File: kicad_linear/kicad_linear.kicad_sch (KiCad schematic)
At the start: 6 parts, among them J1 LObits, J2 HIbits, J3 PGM, U1 ATtiny1616-S, U2 HSN-3621

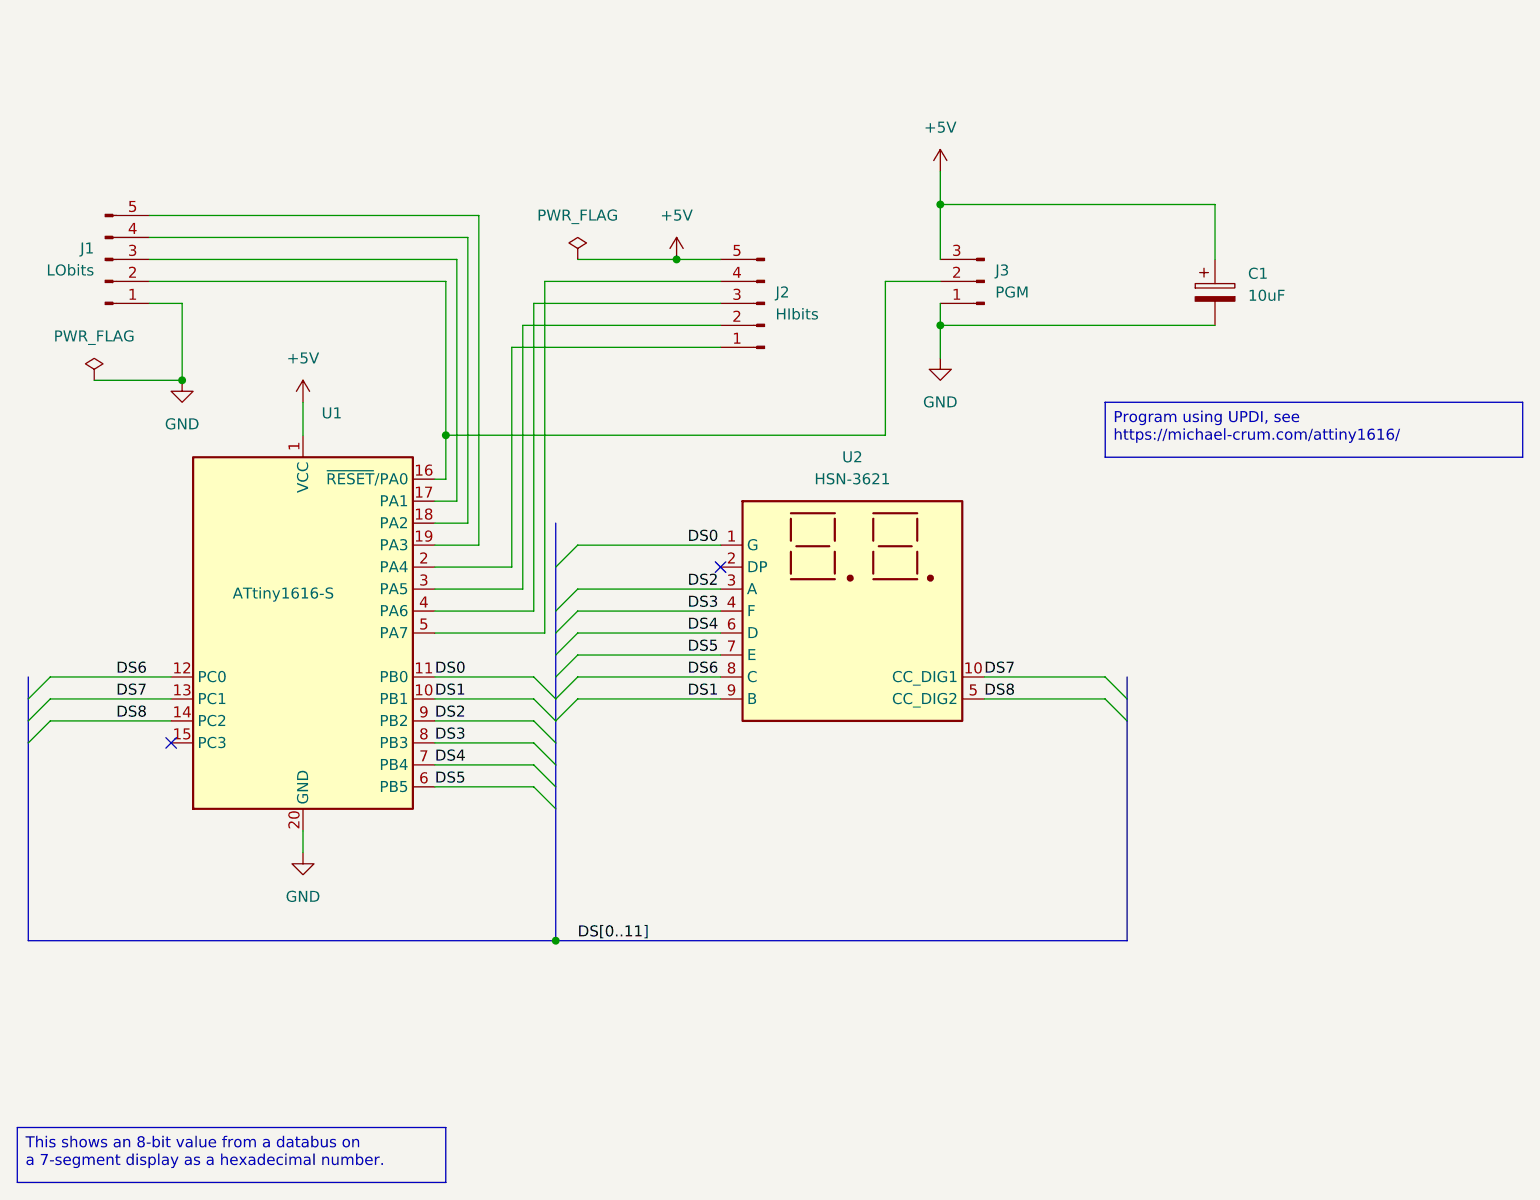
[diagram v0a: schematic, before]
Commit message: Add a linear variant that should be easier to use
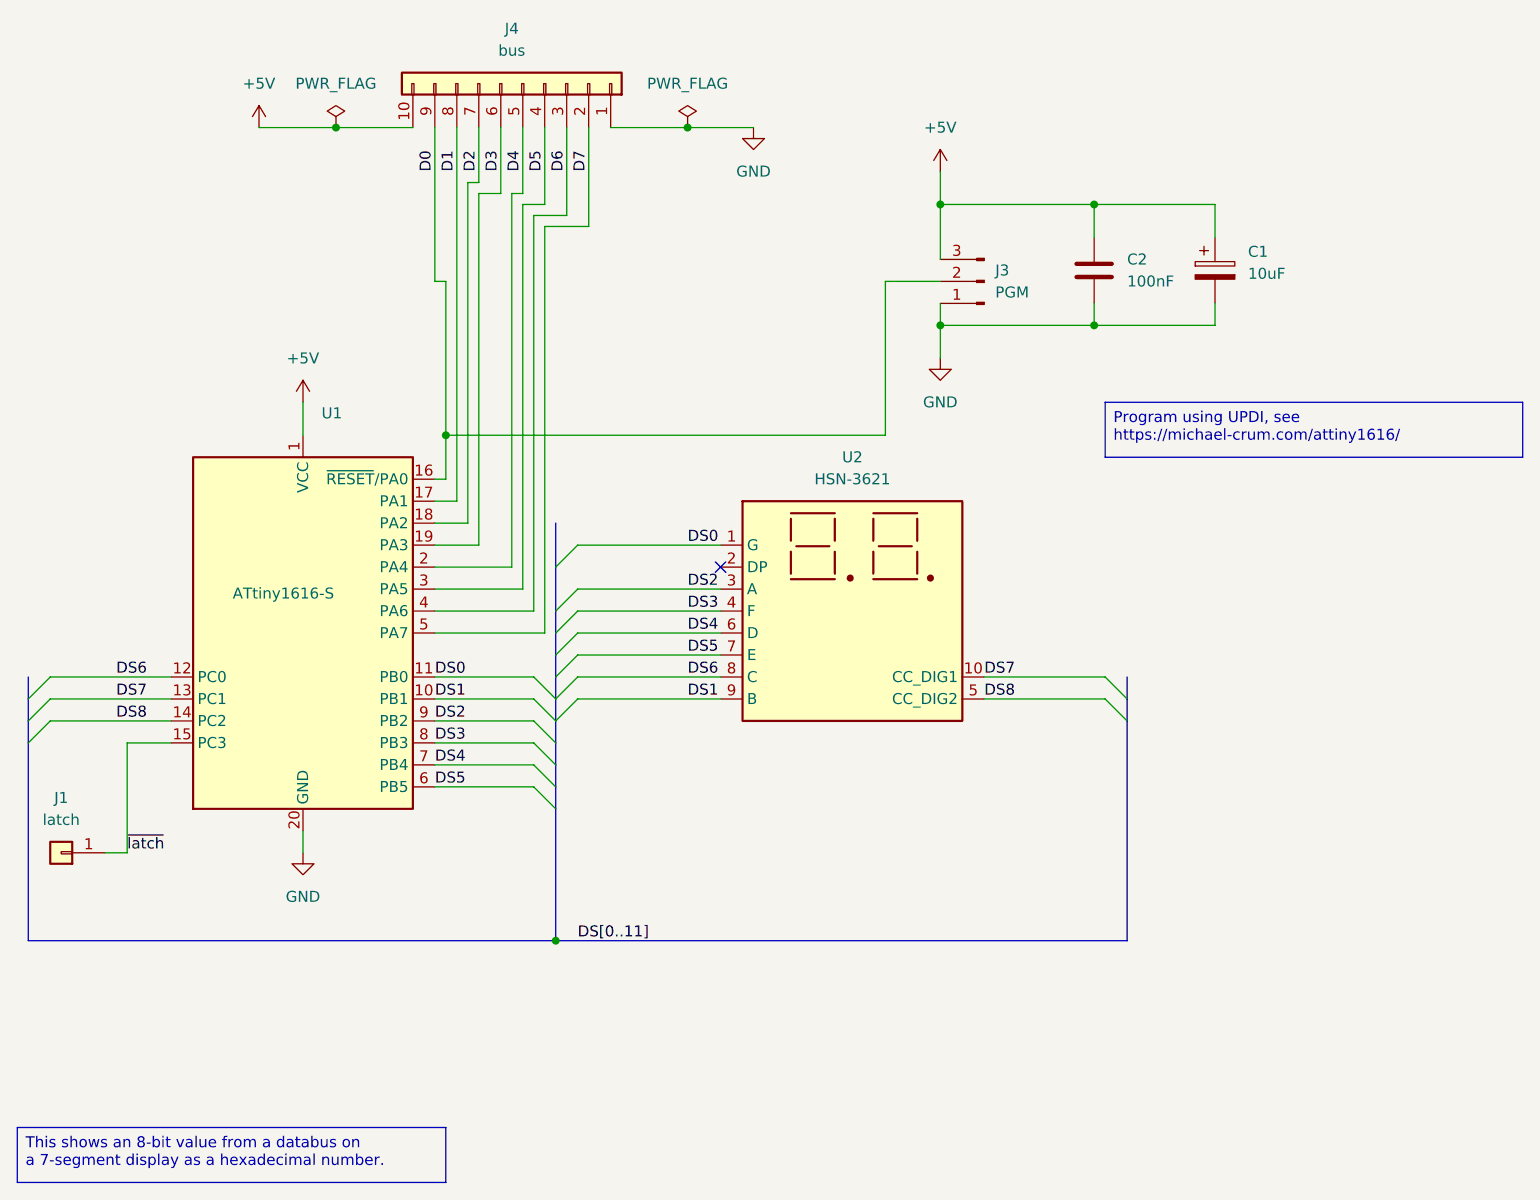
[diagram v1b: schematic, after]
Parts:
- removed J1: LObits, Connector_PinHeader_2.54mm:PinHeader_1x05_P2.54mm_Vertical, symbol Library:Conn_01x05_Pin
- removed J2: HIbits, Connector_PinHeader_2.54mm:PinHeader_1x05_P2.54mm_Vertical, symbol Library:Conn_01x05_Pin
- added C2: 100nF, Capacitor_SMD:C_0805_2012Metric_Pad1.18x1.45mm_HandSolder, symbol Device:C
- added J1: latch, Connector_PinHeader_2.54mm:PinHeader_1x01_P2.54mm_Vertical, symbol Connector_Generic:Conn_01x01
- added J4: bus, Connector_PinHeader_2.54mm:PinHeader_1x10_P2.54mm_Vertical, symbol Connector_Generic:Conn_01x10
- C1: footprint Capacitor_SMD:C_0805_2012Metric -> Capacitor_Tantalum_SMD:CP_EIA-2012-12_Kemet-R_HandSolder
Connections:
- net +5V: now also C2.1, J4.10 (Pin_10)
- net GND: now also C2.2, J4.1 (Pin_1)
- net ~{latch}: now reaches U1.15 (PC3)
- net ~{latch}: now also J1.1 (Pin_1)
- net D0: now reaches J3.2 (Pin_2), U1.16 (~{RESET}/PA0)
- net D0: now also J4.9 (Pin_9)
- net D1: now reaches U1.17 (PA1)
- net D1: now also J4.8 (Pin_8)
- net D2: now reaches U1.18 (PA2)
- net D2: now also J4.7 (Pin_7)
- net D3: now reaches U1.19 (PA3)
- net D3: now also J4.6 (Pin_6)
- net D4: now reaches U1.2 (PA4)
- net D4: now also J4.5 (Pin_5)
- net D5: now reaches U1.3 (PA5)
- net D5: now also J4.4 (Pin_4)
- net D6: now reaches U1.4 (PA6)
- net D6: now also J4.3 (Pin_3)
- net D7: now reaches U1.5 (PA7)
- net D7: now also J4.2 (Pin_2)
- no-connect marks 2 -> 1
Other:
- moved on the sheet: C1

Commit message: Fix capacitor footprint
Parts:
- C1: footprint Capacitor_Tantalum_SMD:CP_EIA-2012-12_Kemet-R_HandSolder -> Capacitor_Tantalum_SMD:CP_EIA-3528-12_Kemet-T_HandSolder
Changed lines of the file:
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@@
 			)
 		)
-		(property "Footprint" "Capacitor_Tantalum_SMD:CP_EIA-2012-12_Kemet-R_HandSolder"
+		(property "Footprint" "Capacitor_Tantalum_SMD:CP_EIA-3528-12_Kemet-T_HandSolder"
 			(at 185.1152 54.61 0)
 			(effects
